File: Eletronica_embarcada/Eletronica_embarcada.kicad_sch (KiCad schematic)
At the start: 93 parts, among them CON2 USB_B, J1 Switch, J3 BOOT_JUMPER, J4 BUZZER, U8 FT232RL

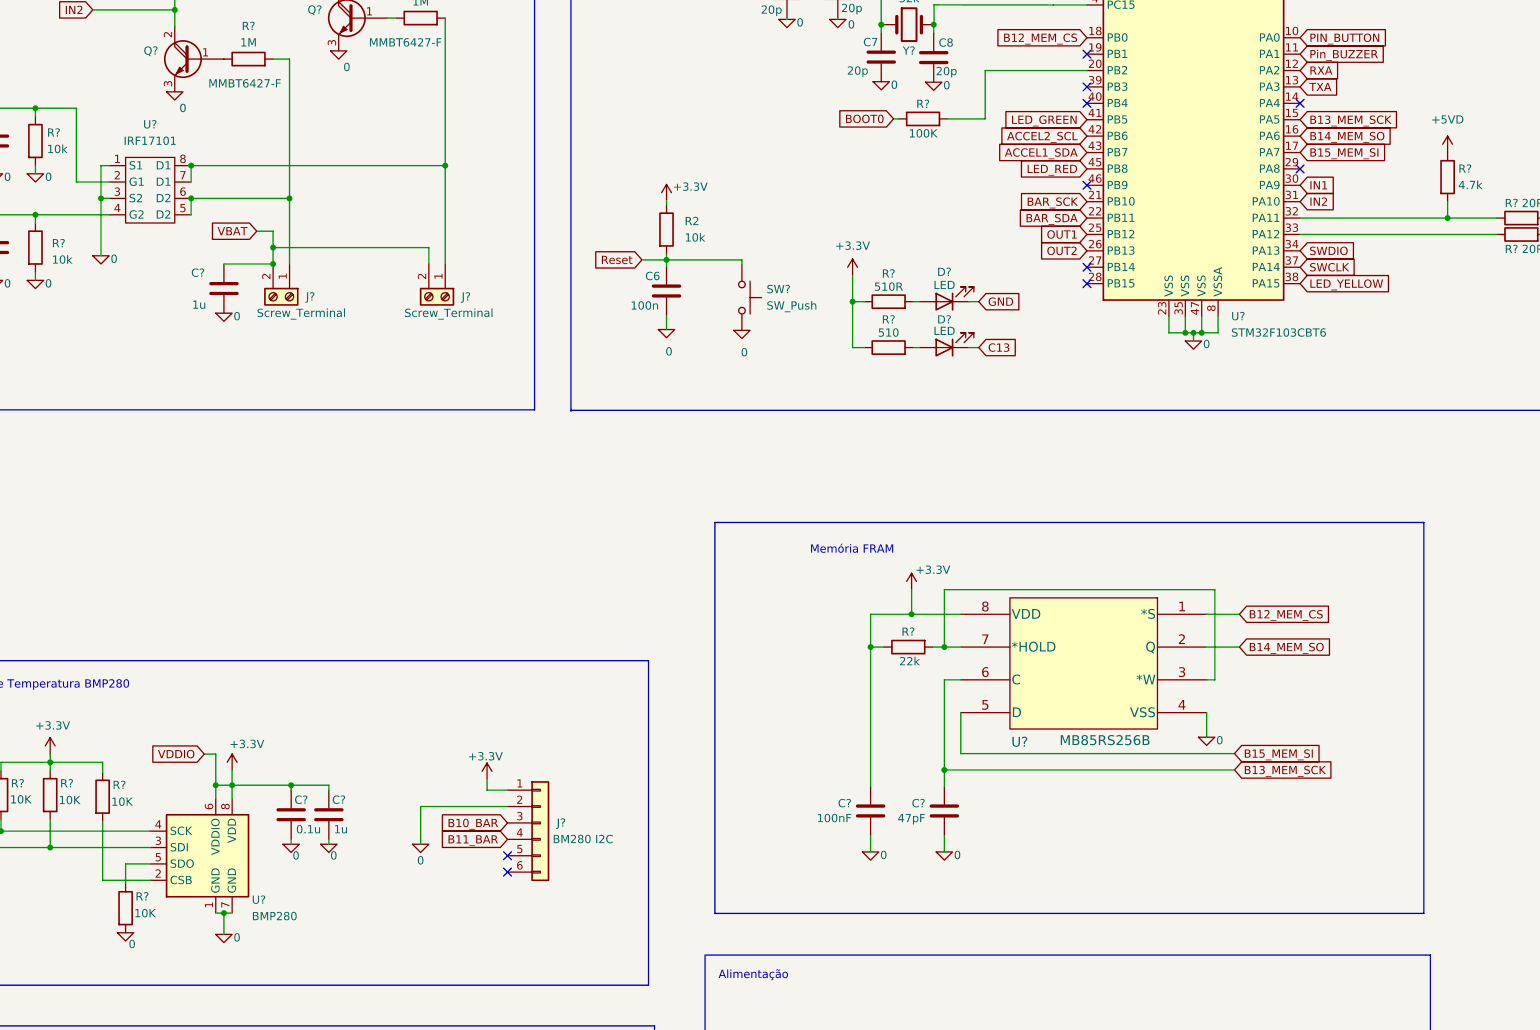
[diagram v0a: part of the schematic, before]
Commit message: esquemático revisado.
necessário adicionar circuito segundo acelerômetro.
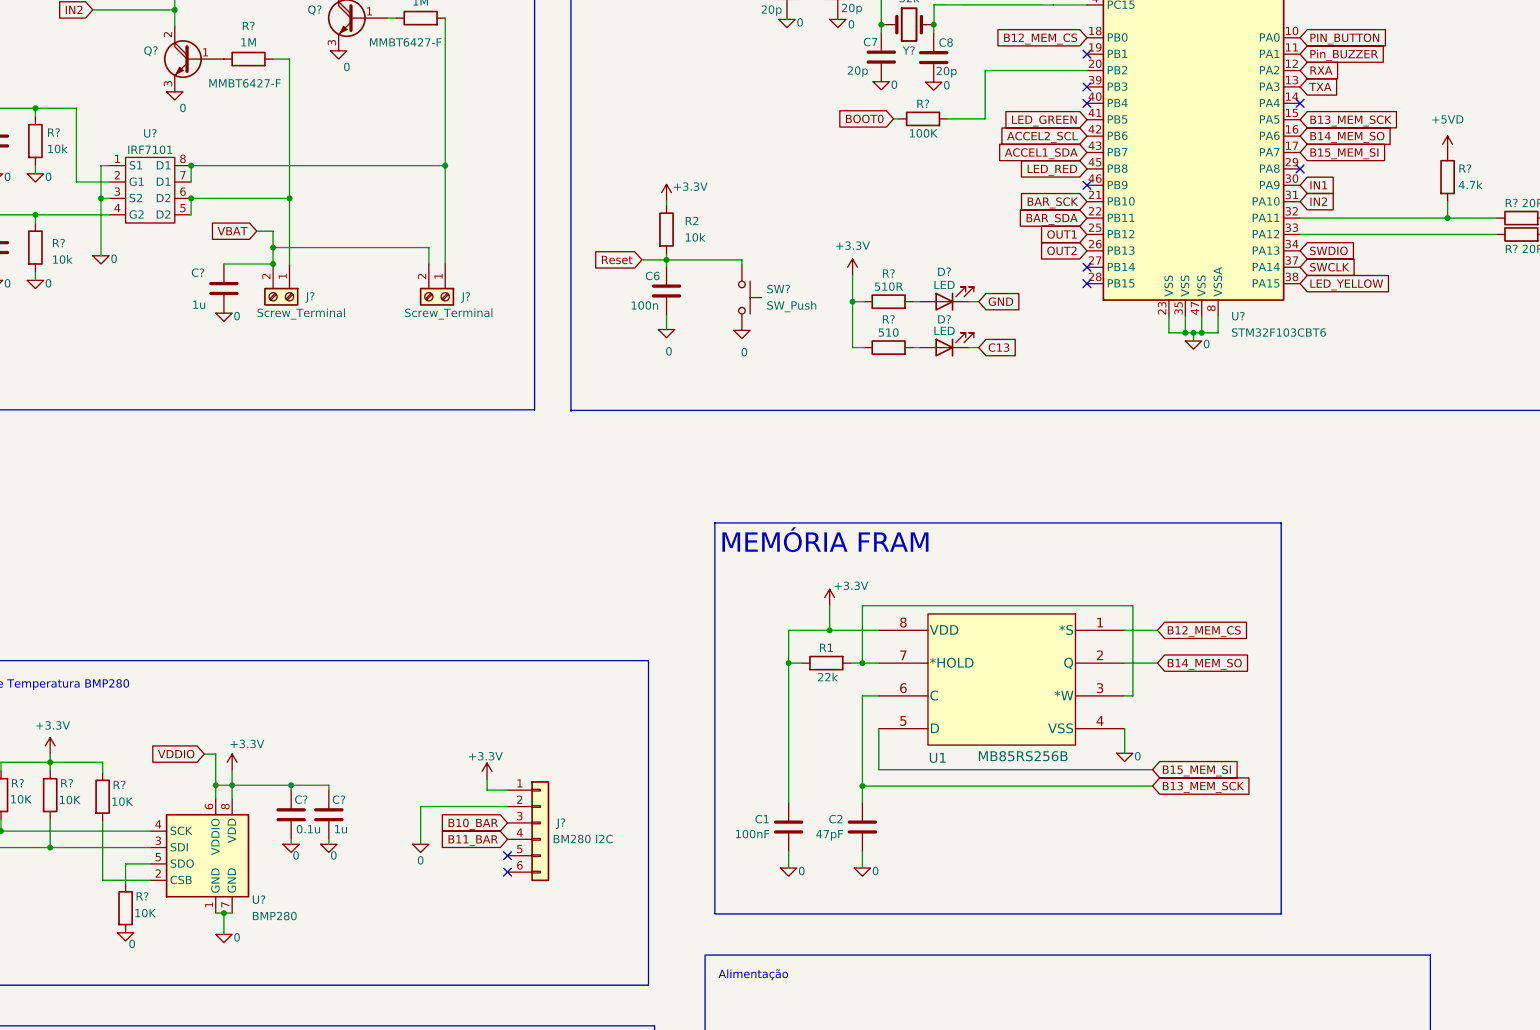
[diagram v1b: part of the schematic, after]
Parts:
- U?: value IRF17101 -> IRF7101
- gave numbers to parts that had none: 4
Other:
- note added: "MEMÓRIA FRAM"
- note removed: "Memória FRAM"
- moved on the sheet: C1, C2, R1, U1

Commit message: finalizado.
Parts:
- removed J?: BM280 I2C, symbol Connector_Generic:Conn_01x06
- removed J?: MPU6050, symbol Connector_Generic:Conn_01x08
- added C15, C18: 0.1uF, Capacitor_SMD:C_0603_1608Metric_Pad1.08x0.95mm_HandSolder, symbol Device:C
- added C16: 0.01uF, Capacitor_SMD:C_0603_1608Metric_Pad1.08x0.95mm_HandSolder, symbol Device:C
- added C17: 2200pF, Capacitor_SMD:C_0603_1608Metric_Pad1.08x0.95mm_HandSolder, symbol Device:C
- added R26, R27, R28: 4.7k, Resistor_SMD:R_0603_1608Metric_Pad0.98x0.95mm_HandSolder, symbol Device:R
- added U5: MPU-6050, Sensor_Motion:InvenSense_QFN-24_4x4mm_P0.5mm, symbol Sensor_Motion:MPU-6050
- C1, C2, C3, C4: footprint (none) -> Capacitor_SMD:C_0603_1608Metric_Pad1.08x0.95mm_HandSolder
- C10, C13, C14, C19, C20, C21, C22, C25, C8, C9: renamed from C?; footprint (none) -> Capacitor_SMD:C_0603_1608Metric_Pad1.08x0.95mm_HandSolder
- C23, C24: renamed from C?; footprint (none) -> Capacitor_SMD:CP_Elec_10x10.5
- C5: renamed from C7; footprint (none) -> Capacitor_SMD:C_0603_1608Metric_Pad1.08x0.95mm_HandSolder
- C6: renamed from C8; footprint (none) -> Capacitor_SMD:C_0603_1608Metric_Pad1.08x0.95mm_HandSolder
- C7: renamed from C6; footprint (none) -> Capacitor_SMD:C_0603_1608Metric_Pad1.08x0.95mm_HandSolder
- CON2: footprint Connector_USB:USB_B_Lumberg_2411_02_Horizontal -> Connector_USB:USB_Micro-B_Molex_47346-0001
- CON2: renamed from J?; footprint (none) -> Connector_USB:USB_Mini-B_Lumberg_2486_01_Horizontal
- CON3: renamed from CON?; footprint bt1:BAT_BH123A -> Connector_JST:JST_EH_B2B-EH-A_1x02_P2.50mm_Vertical
- D1, D2, D4, D5: renamed from D?; footprint (none) -> LED_SMD:LED_0603_1608Metric_Pad1.05x0.95mm_HandSolder
- D3: renamed from D1; footprint (none) -> LED_SMD:LED_0603_1608Metric_Pad1.05x0.95mm_HandSolder
- J1: renamed from J?; footprint (none) -> Connector_JST:JST_XH_B4B-XH-AM_1x04_P2.50mm_Vertical
- J2: renamed from J3; footprint (none) -> Connector_PinHeader_1.00mm:PinHeader_2x03_P1.00mm_Vertical
- J3: renamed from J1; footprint (none) -> Button_Switch_THT:SW_E-Switch_EG1224_SPDT_Angled
- J4: footprint (none) -> Connector_JST:JST_XH_B2B-XH-A_1x02_P2.50mm_Vertical
- J5, J6: renamed from J?; footprint (none) -> Connector_Phoenix_MC:PhoenixContact_MCV_1,5_2-G-3.5_1x02_P3.50mm_Vertical
- Q1, Q2: renamed from Q?; footprint (none) -> Package_TO_SOT_SMD:SOT-23
- R1: footprint (none) -> Resistor_SMD:R_0603_1608Metric_Pad0.98x0.95mm_HandSolder
- R10, R11, R12, R13, R14, R15, R16, R19, R2, R20, R21, R29, R3, R30, R31, R4, R5, R7, R8, R9: renamed from R?; footprint (none) -> Resistor_SMD:R_0603_1608Metric_Pad0.98x0.95mm_HandSolder
- R18: renamed from R3; footprint (none) -> Resistor_SMD:R_0603_1608Metric_Pad0.98x0.95mm_HandSolder
- R6: renamed from R2; footprint (none) -> Resistor_SMD:R_0603_1608Metric_Pad0.98x0.95mm_HandSolder
- SW1: renamed from SW?; footprint (none) -> Button_Switch_SMD:SW_SPST_CK_RS282G05A3
- U2: renamed from U?; footprint (none) -> Package_SO:SOIC-8_3.9x4.9mm_P1.27mm
- U3: renamed from U1; footprint 4:FM25V10-GTR -> Package_SO:SOIC-8_3.9x4.9mm_P1.27mm
- Y1: renamed from Y?; footprint (none) -> Crystal:Crystal_SMD_HC49-SD
- Y2: renamed from Y?; footprint (none) -> Crystal:Crystal_SMD_SeikoEpson_MA406-4Pin_11.7x4.0mm
- gave numbers to parts that had none: 19
- renumbered C1 to C11, C2 to C12, R1 to R17
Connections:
- net BAR_SCK is gone; now on net ACCEL2_SCL: R22.2, U1.21 (PB10), U4.4 (SCK)
- net +3.3V: now also C15.1, C16.1, R26.1, R27.1, U5.13 (VDD), U5.8 (VDDIO)
- net 0: now also C15.2, C16.2, C17.2, C18.2, R28.2, U5.1 (CLKIN), U5.11 (FSYNC), U5.18 (GND)
- net ACCEL1_SDA: now also R27.2, U5.24 (SDA); no longer R30.2, U6.24 (SDA)
- net ACCEL2_SCL: now also R26.2, U5.23 (SCL); no longer U1.42 (PB6)
- net BAR_SDA renamed ACCEL2_SDA
- net ACCEL2_SDA: now also R30.2, U6.24 (SDA)
- new net: R28.1, U5.9 (AD0)
- new net: C17.1, U5.20 (CPOUT)
- new net: C18.1, U5.10 (REGOUT)
- new net ACCEL1_SCL: U1.42 (PB6)
- no-connect marks 31 -> 28
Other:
- note added: "ACELERÔMETRO MPU6050"
- note added: "ACELERÔMETRO MPU6050 ROTACIONADO"
- note added: "ALIMENTAÇÃO"
- note added: "BOTÃO LANÇAMENTO"
- note added: "BUZZER"
- note added: "CONVERSOR USB/SERIAL"
- note added: "GRAVAÇÃO ST-LINK"
- note added: "LED STATUS"
- note added: "SENSOR BMP280"
- note removed: "ACELERÔMETRO"
- note removed: "Alimentação"
- note removed: "BOTÃO PARA LANÇAMENTO"
- note removed: "BUZZER INFO"
- note removed: "CONVERSOR SERIAL/USB"
- note removed: "GRAVAÇÃO BLUEPILL STLINK"
- note removed: "LED STATUS FOGUETE"
- note removed: "Módulo Sensor de Pressão e Temperatura BMP280"
- company: (none) -> Universidade Estadual de Londrina
- title: (none) -> Computador de Bordo - RBBoard
- moved on the sheet: C1, C10, C11, C12, C13, C14, C19, C2, C20, C21, C22, C23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

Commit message: att
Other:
- moved on the sheet: J4, Q3, R21
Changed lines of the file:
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@@
   (junction (at 197.231 228.1936) (diameter 0) (color 0 0 0 0)
   )
-  (junction (at 195.58 297.815) (diameter 0) (color 0 0 0 0)
+  (junction (at 206.248 276.606) (diameter 0) (color 0 0 0 0)
   )
   (junction (at 56.261 354.965) (diameter 0) (color 0 0 0 0)
@@
   (junction (at 109.22 67.437) (diameter 0) (color 0 0 0 0)
   )
-  (junction (at 195.58 287.909) (diameter 0) (color 0 0 0 0)
+  (junction (at 206.248 266.7) (diameter 0) (color 0 0 0 0)
   )
   (junction (at 85.09 72.517) (diameter 0) (color 0 0 0 0)
@@
     (stroke (width 0) (type default))
   )
-  (wire (pts (xy 200.152 293.751) (xy 203.962 293.751))
+  (wire (pts (xy 210.82 272.542) (xy 214.63 272.542))
     (stroke (width 0) (type default))
   )
@@
     (stroke (width 0) (type default))
   )
-  (wire (pts (xy 200.152 293.751) (xy 200.152 297.815))
+  (wire (pts (xy 210.82 272.542) (xy 210.82 276.606))
     (stroke (width 0) (type default))
   )
@@
     (stroke (width 0) (type default))
   )
-  (polyline (pts (xy 220.726 314.071) (xy 171.45 314.071))
+  (polyline (pts (xy 231.394 292.862) (xy 182.118 292.862))
     (stroke (width 0) (type default))
   )
-  (wire (pts (xy 200.152 291.211) (xy 200.152 287.909))
+  (wire (pts (xy 210.82 270.002) (xy 210.82 266.7))
     (stroke (width 0) (type default))
   )
@@
     (stroke (width 0) (type default))
   )
-  (wire (pts (xy 195.58 311.023) (xy 195.58 309.245))
+  (wire (pts (xy 206.248 289.814) (xy 206.248 288.036))
     (stroke (width 0) (type default))
   )
@@
     (stroke (width 0) (type default))
   )
-  (wire (pts (xy 195.58 297.815) (xy 195.58 296.545))
+  (wire (pts (xy 206.248 276.606) (xy 206.248 275.336))
     (stroke (width 0) (type default))
   )
@@
     (stroke (width 0) (type default))
   )
-  (wire (pts (xy 187.706 304.165) (xy 187.96 304.165))
+  (wire (pts (xy 198.374 282.956) (xy 198.628 282.956))
     (stroke (width 0) (type default))
   )
@@
     (stroke (width 0) (type default))
   )
-  (wire (pts (xy 195.58 287.909) (xy 195.58 288.925))
+  (wire (pts (xy 206.248 266.7) (xy 206.248 267.716))
     (stroke (width 0) (type default))
   )
@@
     (stroke (width 0) (type default))
   )
-  (polyline (pts (xy 220.726 282.194) (xy 220.726 314.071))
+  (polyline (pts (xy 231.394 260.985) (xy 231.394 292.862))
     (stroke (width 0) (type default))
   )
@@
     (stroke (width 0) (type default))
   )
-  (wire (pts (xy 203.962 291.211) (xy 200.152 291.211))
+  (wire (pts (xy 214.63 270.002) (xy 210.82 270.002))
     (stroke (width 0) (type default))
   )
@@
     (stroke (width 0) (type default))
   )
-  (polyline (pts (xy 171.45 282.321) (xy 171.45 314.071))
+  (polyline (pts (xy 182.118 261.112) (xy 182.118 292.862))
     (stroke (width 0) (type default))
   )
@@
     (stroke (width 0) (type default))
   )
-  (wire (pts (xy 200.152 297.815) (xy 195.58 297.815))
+  (wire (pts (xy 210.82 276.606) (xy 206.248 276.606))
     (stroke (width 0) (type default))
   )
@@
     (stroke (width 0) (type default))
   )
-  (wire (pts (xy 200.152 287.909) (xy 195.58 287.909))
+  (wire (pts (xy 210.82 266.7) (xy 206.248 266.7))
     (stroke (width 0) (type default))
   )
@@
     (stroke (width 0) (type default))
   )
-  (wire (pts (xy 195.58 297.815) (xy 195.58 299.085))
+  (wire (pts (xy 206.248 276.606) (xy 206.248 277.876))
     (stroke (width 0) (type default))
   )
@@
     (stroke (width 0) (type default))
   )
-  (wire (pts (xy 195.58 286.639) (xy 195.58 287.909))
+  (wire (pts (xy 206.248 265.43) (xy 206.248 266.7))
     (stroke (width 0) (type default))
   )
@@
     (stroke (width 0) (type default))
   )
-  (polyline (pts (xy 171.45 282.194) (xy 220.726 282.194))
+  (polyline (pts (xy 182.118 260.985) (xy 231.394 260.985))
     (stroke (width 0) (type default))
   )
@@
     (effects (font (size 3 3)) (justify left bottom))
   )
-  (text "BUZZER\n" (at 172.339 286.893 0)
+  (text "BUZZER\n" (at 183.007 265.684 0)
     (effects (font (size 3 3)) (justify left bottom))
   )
@@
     )
   )
-  (global_label "Pin_BUZZER" (shape input) (at 187.706 304.165 180) (fields_autoplaced)
+  (global_label "Pin_BUZZER" (shape input) (at 198.374 282.956 180) (fields_autoplaced)
     (effects (font (size 1.27 1.27)) (justify right))
-    (property "Intersheetrefs" "${INTERSHEET_REFS}" (at 173.8629 304.0856 0)
+    (property "Intersheetrefs" "${INTERSHEET_REFS}" (at 184.5309 282.8766 0)
       (effects (font (size 1.27 1.27)) (justify right) hide)
     )
@@
     )
   )
-  (symbol (lib_id "Connector_Generic:Conn_01x02") (at 209.042 291.211 0) (unit 1)
+  (symbol (lib_id "Connector_Generic:Conn_01x02") (at 219.71 270.002 0) (unit 1)
     (in_bom yes) (on_board yes) (dnp no) (fields_autoplaced)
-    (property "Reference" "J4" (at 212.09 291.2109 0)
+    (property "Reference" "J4" (at 222.758 270.0019 0)
       (effects (font (size 1.27 1.27)) (justify left))
     )
-    (property "Value" "BUZZER" (at 212.09 293.7509 0)
+    (property "Value" "BUZZER" (at 222.758 272.5419 0)
       (effects (font (size 1.27 1.27)) (justify left))
     )
-    (property "Footprint" "Connector_JST:JST_XH_B2B-XH-A_1x02_P2.50mm_Vertical" (at 209.042 291.211 0)
+    (property "Footprint" "Connector_JST:JST_XH_B2B-XH-A_1x02_P2.50mm_Vertical" (at 219.71 270.002 0)
       (effects (font (size 1.27 1.27)) hide)
     )
-    (property "Datasheet" "~" (at 209.042 291.211 0)
+    (property "Datasheet" "~" (at 219.71 270.002 0)
       (effects (font (size 1.27 1.27)) hide)
     )
@@
     )
   )
-  (symbol (lib_id "Transistor_BJT:BC817") (at 193.04 304.165 0) (unit 1)
+  (symbol (lib_id "Transistor_BJT:BC817") (at 203.708 282.956 0) (unit 1)
     (in_bom yes) (on_board yes) (dnp no) (fields_autoplaced)
-    (property "Reference" "Q3" (at 198.755 303.53 0)
+    (property "Reference" "Q3" (at 209.423 282.321 0)
       (effects (font (size 1.27 1.27)) (justify left))
     )
-    (property "Value" "BC817" (at 198.755 306.07 0)
+    (property "Value" "BC817" (at 209.423 284.861 0)
       (effects (font (size 1.27 1.27)) (justify left))
     )
-    (property "Footprint" "Package_TO_SOT_SMD:SOT-23" (at 198.12 306.07 0)
+    (property "Footprint" "Package_TO_SOT_SMD:SOT-23" (at 208.788 284.861 0)
       (effects (font (size 1.27 1.27) italic) (justify left) hide)
     )
-    (property "Datasheet" "https://www.onsemi.com/pub/Collateral/BC818-D.pdf" (at 193.04 304.165 0)
+    (property "Datasheet" "https://www.onsemi.com/pub/Collateral/BC818-D.pdf" (at 203.708 282.956 0)
       (effects (font (size 1.27 1.27)) (justify left) hide)
     )
@@
     )
   )
-  (symbol (lib_id "Device:R") (at 195.58 292.735 180) (unit 1)
+  (symbol (lib_id "Device:R") (at 206.248 271.526 180) (unit 1)
     (in_bom yes) (on_board yes) (dnp no)
-    (property "Reference" "R21" (at 189.611 291.084 0)
+    (property "Reference" "R21" (at 200.279 269.875 0)
       (effects (font (size 1.27 1.27)) (justify right))
     )
-    (property "Value" "1,5k" (at 189.484 294.005 0)
+    (property "Value" "1,5k" (at 200.152 272.796 0)
       (effects (font (size 1.27 1.27)) (justify right))
     )
-    (property "Footprint" "Resistor_SMD:R_0603_1608Metric_Pad0.98x0.95mm_HandSolder" (at 197.358 292.735 90)
+    (property "Footprint" "Resistor_SMD:R_0603_1608Metric_Pad0.98x0.95mm_HandSolder" (at 208.026 271.526 90)
       (effects (font (size 1.27 1.27)) hide)
     )
-    (property "Datasheet" "~" (at 195.58 292.735 0)
+    (property "Datasheet" "~" (at 206.248 271.526 0)
       (effects (font (size 1.27 1.27)) hide)
     )
@@
     )
   )
-  (symbol (lib_id "pspice:0") (at 195.58 311.023 0) (unit 1)
+  (symbol (lib_id "pspice:0") (at 206.248 289.814 0) (unit 1)
     (in_bom yes) (on_board yes) (dnp no)
-    (property "Reference" "#GND0148" (at 195.58 313.563 0)
+    (property "Reference" "#GND0148" (at 206.248 292.354 0)
       (effects (font (size 1.27 1.27)) hide)
     )
-    (property "Value" "0" (at 197.358 312.293 0)
+    (property "Value" "0" (at 208.026 291.084 0)
       (effects (font (size 1.27 1.27)))
     )
-    (property "Footprint" "" (at 195.58 311.023 0)
+    (property "Footprint" "" (at 206.248 289.814 0)
       (effects (font (size 1.27 1.27)) hide)
     )
-    (property "Datasheet" "~" (at 195.58 311.023 0)
+    (property "Datasheet" "~" (at 206.248 289.814 0)
       (effects (font (size 1.27 1.27)) hide)
     )
@@
     )
   )
-  (symbol (lib_id "power:+5V") (at 195.58 286.639 0) (unit 1)
+  (symbol (lib_id "power:+5V") (at 206.248 265.43 0) (unit 1)
     (in_bom yes) (on_board yes) (dnp no)
-    (property "Reference" "#PWR0121" (at 195.58 290.449 0)
+    (property "Reference" "#PWR0121" (at 206.248 269.24 0)
       (effects (font (size 1.27 1.27)) hide)
     )
-    (property "Value" "+5V" (at 190.5 284.607 0)
+    (property "Value" "+5V" (at 201.168 263.398 0)
       (effects (font (size 1.27 1.27)) (justify left))
     )
-    (property "Footprint" "" (at 195.58 286.639 0)
+    (property "Footprint" "" (at 206.248 265.43 0)
       (effects (font (size 1.27 1.27)) hide)
     )
-    (property "Datasheet" "" (at 195.58 286.639 0)
+    (property "Datasheet" "" (at 206.248 265.43 0)
       (effects (font (size 1.27 1.27)) hide)
     )
